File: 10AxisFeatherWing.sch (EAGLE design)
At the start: 21 parts, among them U1 BNO055, U2 BME280, Y1 32.768kHz

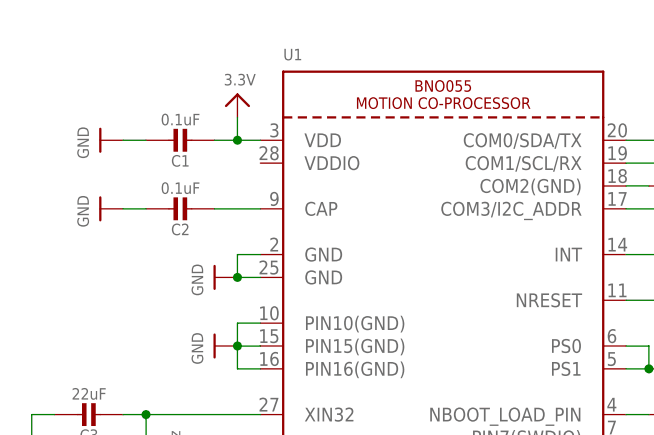
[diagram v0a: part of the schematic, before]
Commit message: Fixed IMU VDDIO not connected
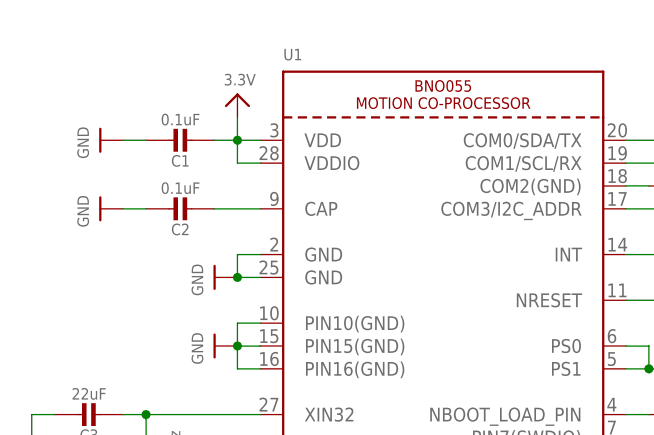
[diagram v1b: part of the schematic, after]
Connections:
- net 3.3V: now also U1.VDDIO
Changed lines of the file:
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@@
 <wire x1="48.26" y1="139.7" x2="50.8" y2="139.7" width="0.1524" layer="91"/>
 <junction x="50.8" y="139.7"/>
+<pinref part="U1" gate="G$1" pin="VDDIO"/>
+<wire x1="53.34" y1="137.16" x2="50.8" y2="137.16" width="0.1524" layer="91"/>
+<wire x1="50.8" y1="137.16" x2="50.8" y2="139.7" width="0.1524" layer="91"/>
 </segment>
 <segment>

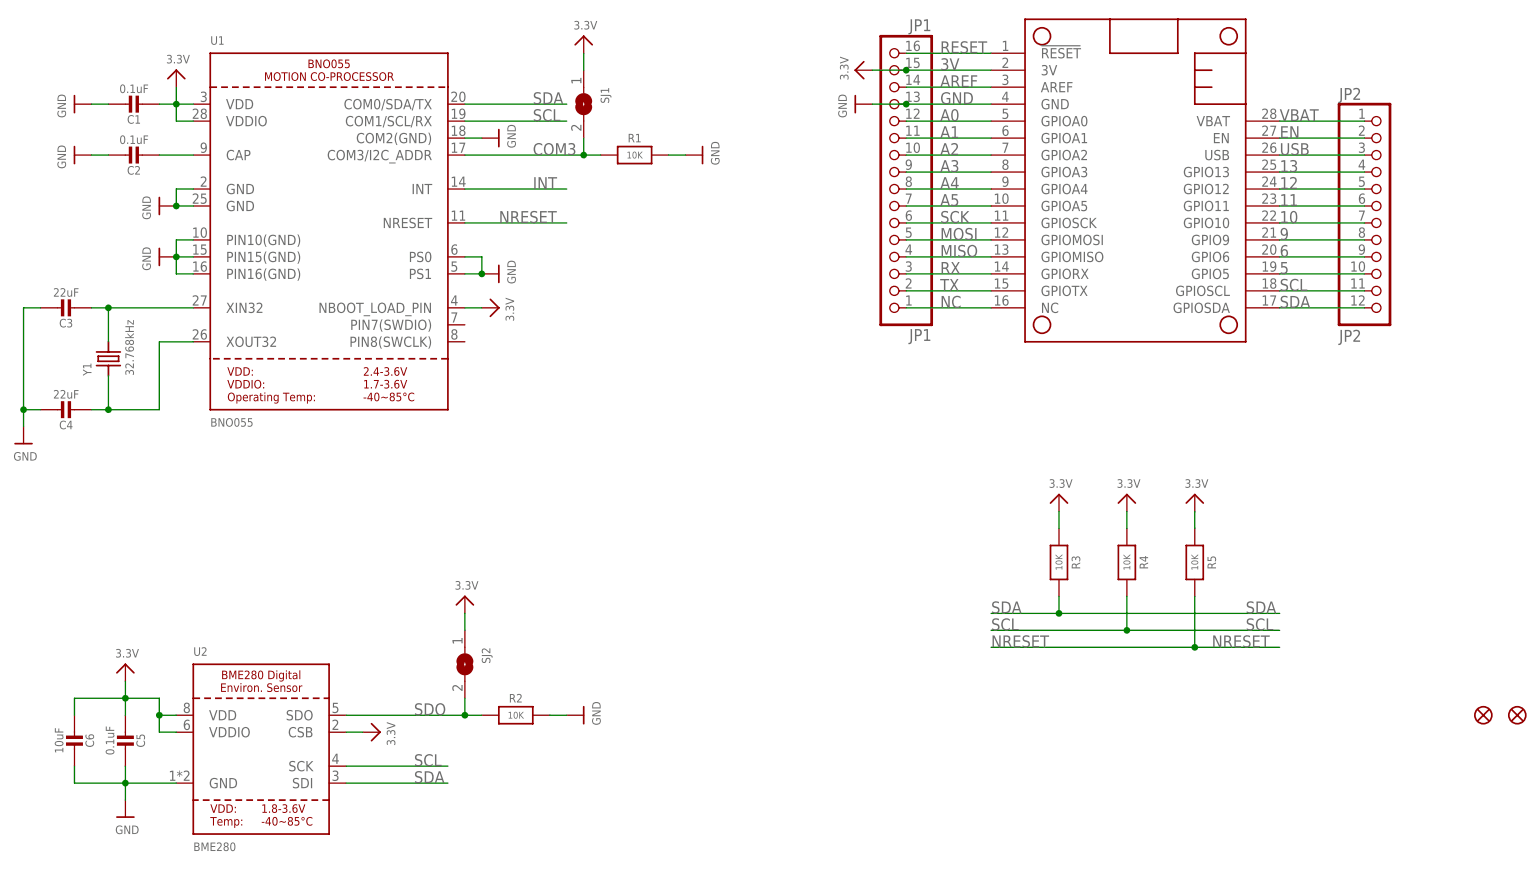
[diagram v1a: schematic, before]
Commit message: Added new features
Added RESET button, INT breakout, and silk text.
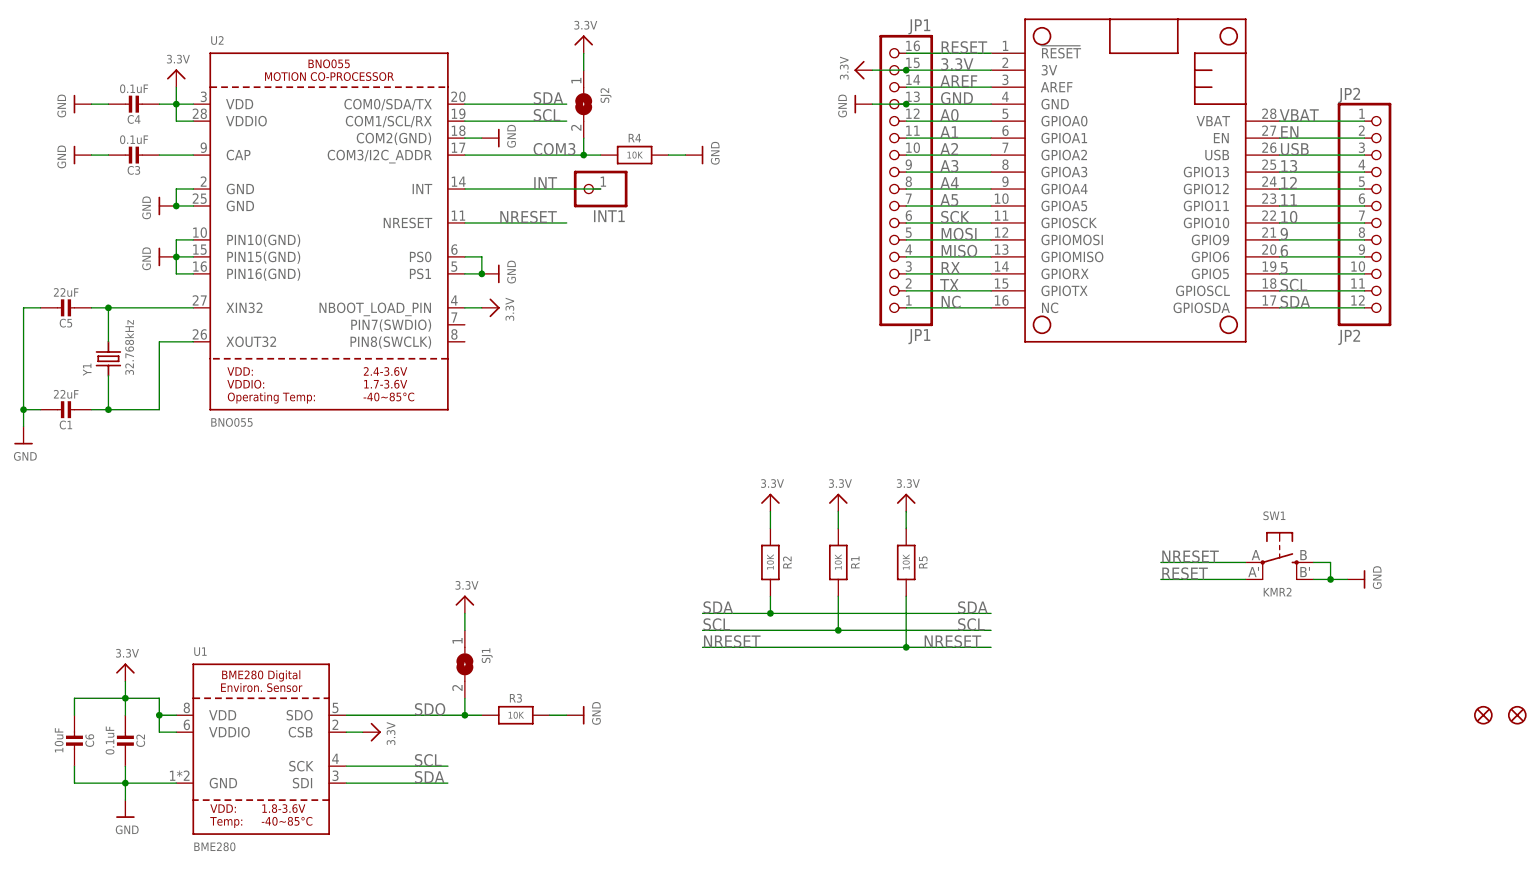
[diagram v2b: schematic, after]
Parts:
- added INT1: (no value), microbuilder:HEADER-1X1ROUND
- added SW1: KMR2, microbuilder:SWITCH_TACT_SMT4.6X2.8
- C1, C5: value 0.1uF -> 22uF
- C3, C4: value 22uF -> 0.1uF
- U1: value BNO055 -> BME280; device microbuilder:BNO055 -> microbuilder:BME280; SPICEPREFIX X -> (none)
- U2: value BME280 -> BNO055; device microbuilder:BME280 -> microbuilder:BNO055; SPICEPREFIX (none) -> X
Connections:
- removed net 3V: JP1.15, MS1.3V
- net 3.3V: now also C2.2, C4.2, JP1.15, MS1.3V, R1.1, R2.1, U1.CSB, U2.NBOOT_LOAD_PIN; no longer C1.2, C5.2, R3.1, R4.1, U1.NBOOT_LOAD_PIN, U2.CSB
- net CAP: now also C3.2, U2.CAP; no longer C2.2, U1.CAP
- net COM3: now also R4.1, SJ2.2, U2.COM3/I2C_ADDR; no longer R1.1, SJ1.2, U1.COM3/I2C_ADDR
- net GND: now also R3.2, R4.2, SW1.S, SW1.S1, U1.GND, U2.COM2(GND), U2.GND@1, U2.GND@2, U2.PIN10(GND), U2.PIN15(GND), U2.PIN16(GND), U2.PS0, U2.PS1; no longer R1.2, R2.2, U1.COM2(GND), U1.GND@1, U1.GND@2, U1.PIN10(GND), U1.PIN15(GND), U1.PIN16(GND), U1.PS0, U1.PS1, U2.GND
- net INT: now also INT1.1, U2.INT; no longer U1.INT
- net NRESET: now also SW1.P, U2.NRESET; no longer U1.NRESET
- net RESET: now also SW1.P1
- net SCL: now also R1.2, U1.SCK, U2.COM1/SCL/RX; no longer R4.2, U1.COM1/SCL/RX, U2.SCK
- net SDA: now also R2.2, U1.SDI, U2.COM0/SDA/TX; no longer R3.2, U1.COM0/SDA/TX, U2.SDI
- net SDO: now also R3.1, SJ1.2, U1.SDO; no longer R2.1, SJ2.2, U2.SDO
- net XIN32: now also C5.2, U2.XIN32; no longer C3.2, U1.XIN32
- net XOUT32: now also C1.2, U2.XOUT32; no longer C4.2, U1.XOUT32
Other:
- moved on the sheet: C1, C2, C3, C4, C5, R1, R2, R3, R4, R5, SJ1, SJ2

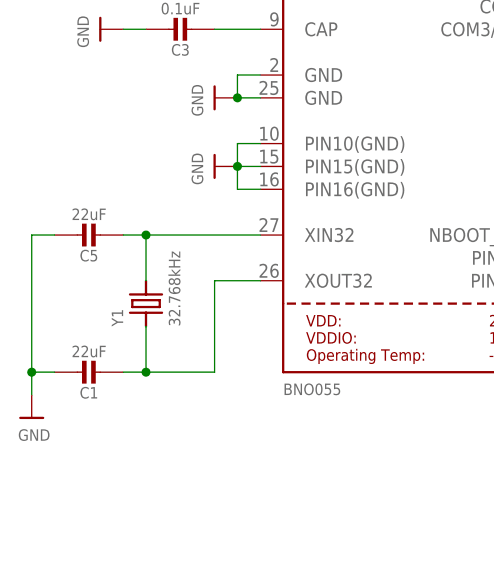
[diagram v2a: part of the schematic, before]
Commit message: Corrected crystal capacitor values
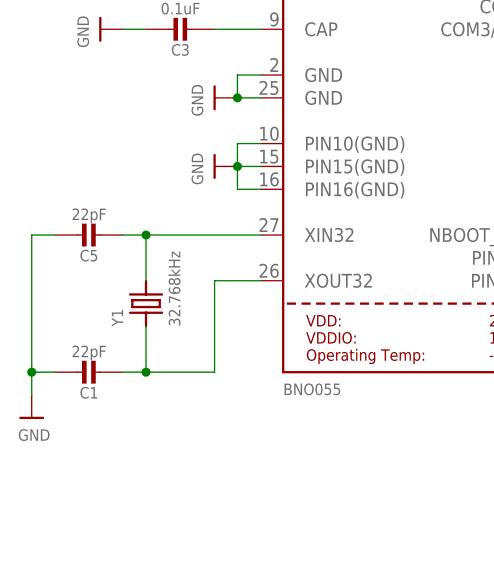
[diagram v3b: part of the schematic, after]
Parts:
- C1, C5: value 22uF -> 22pF
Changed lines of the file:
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@@
 <attribute name="SPICEGROUND" value=""/>
 </part>
-<part name="C5" library="microbuilder" deviceset="CAP_CERAMIC" device="0603_NO" value="22uF">
+<part name="C5" library="microbuilder" deviceset="CAP_CERAMIC" device="0603_NO" value="22pF">
 <spice>
 <pinmapping isusermap="yes" isdevicewide="yes">
@@
 <attribute name="SPICEPREFIX" value="C"/>
 </part>
-<part name="C1" library="microbuilder" deviceset="CAP_CERAMIC" device="0603_NO" value="22uF">
+<part name="C1" library="microbuilder" deviceset="CAP_CERAMIC" device="0603_NO" value="22pF">
 <spice>
 <pinmapping isusermap="yes" isdevicewide="yes">
